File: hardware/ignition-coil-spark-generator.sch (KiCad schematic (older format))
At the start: 16 parts

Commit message: Smaller resistors, trying to make optocoupler act faster
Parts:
- R?: value 10 k -> 270
- R?: value 1 k -> 270
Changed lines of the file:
@@
 P 6000 3750
 F 0 "R?" V 6080 3750 50  0000 C CNN
-F 1 "10 k" V 6000 3750 50  0000 C CNN
+F 1 "270" V 6000 3750 50  0000 C CNN
 F 2 "" V 5930 3750 50  0000 C CNN
 F 3 "" H 6000 3750 50  0000 C CNN
@@
 P 4750 4200
 F 0 "R?" V 4830 4200 50  0000 C CNN
-F 1 "1 k" V 4750 4200 50  0000 C CNN
+F 1 "270" V 4750 4200 50  0000 C CNN
 F 2 "" V 4680 4200 50  0000 C CNN
 F 3 "" H 4750 4200 50  0000 C CNN
@@
 $EndComp
 Wire Wire Line
-	5850 3900 6200 3900
+	5850 3900 6000 3900
+Wire Wire Line
+	6000 3900 6200 3900
 $Comp
 L +9V #PWR?

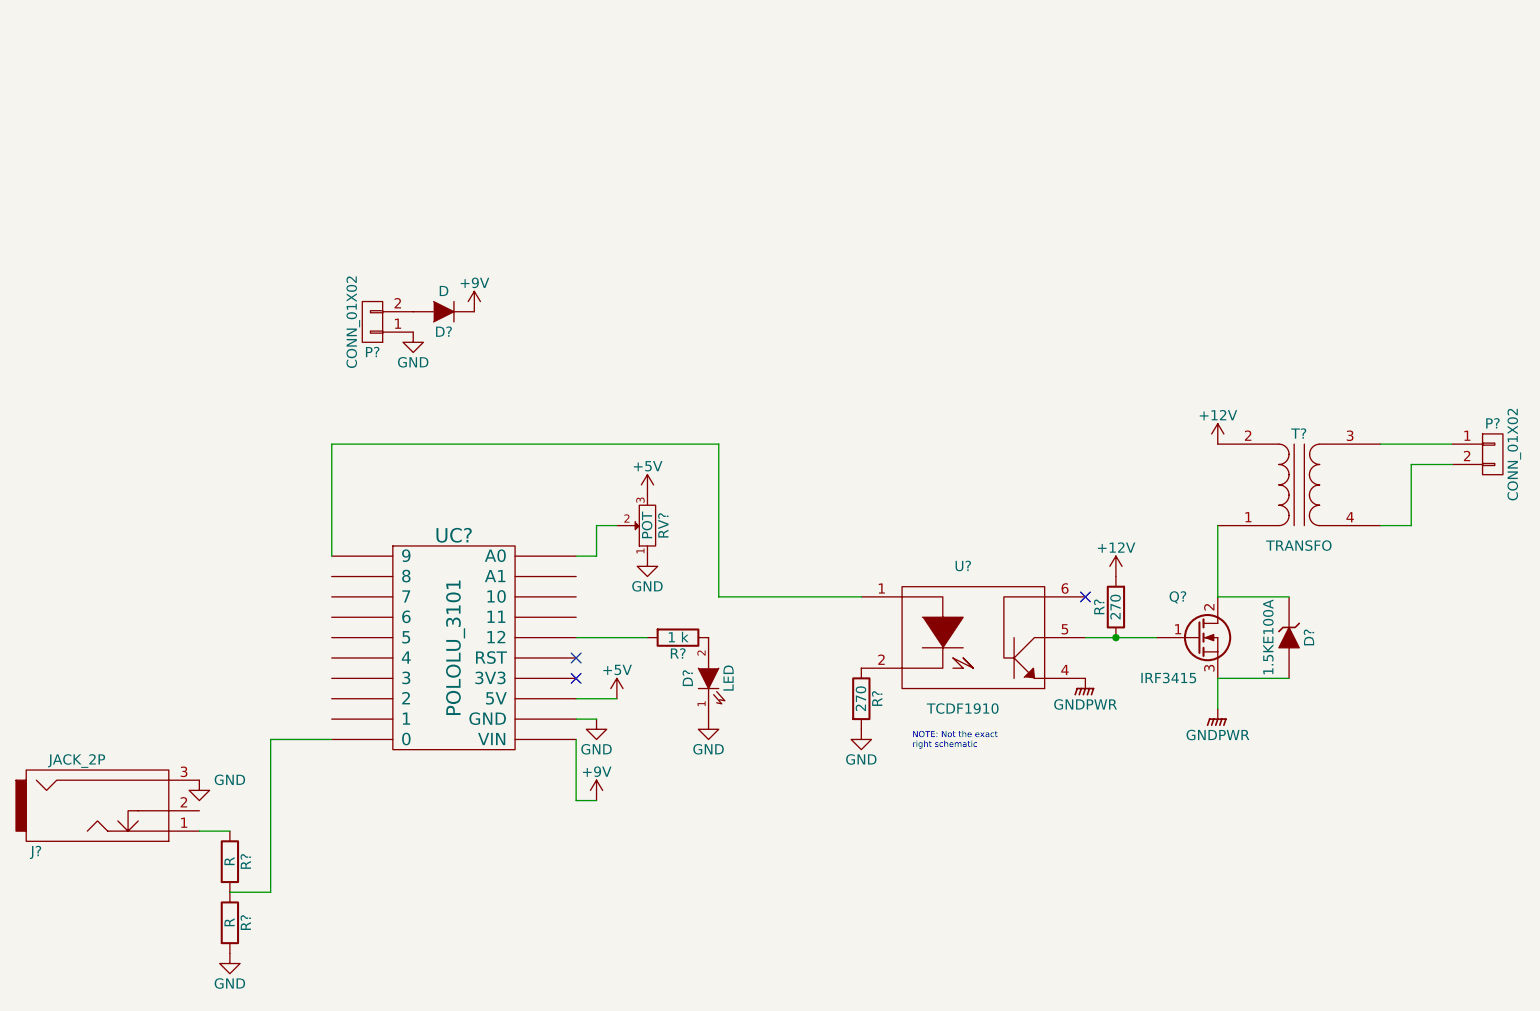
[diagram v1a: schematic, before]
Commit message: New schematic for simplified double ladder generator
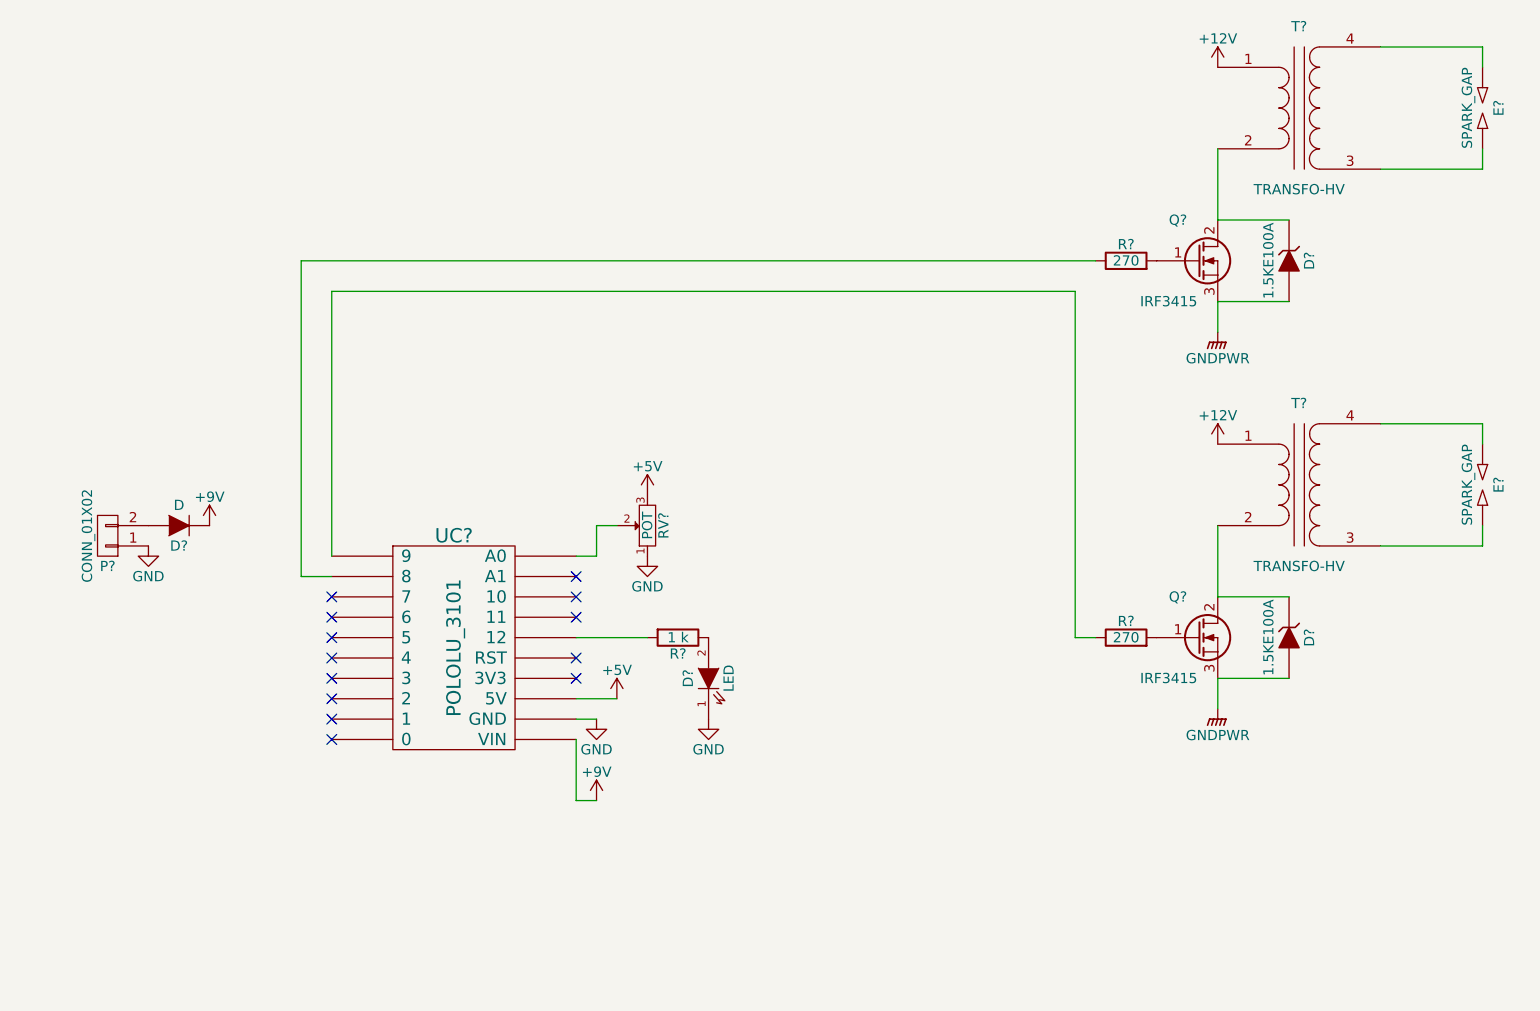
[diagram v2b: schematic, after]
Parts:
- removed J?: JACK_2P, symbol JACK_2P
- removed P?: CONN_01X02, symbol CONN_01X02
- removed R?: 270, symbol R
- removed R? (x2): R, symbol R
- removed T?: TRANSFO, symbol TRANSFO
- removed U?: TCDF1910, symbol PHTRANS
- added D?: 1.5KE100A, symbol ZENER
- added E? (x2): SPARK_GAP, symbol SPARK_GAP
- added Q?: IRF3415, symbol Q_NMOS_GDS
- added R?: 270, symbol R
- added T? (x2): TRANSFO-HV, symbol TRANSFO-HV
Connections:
- net +12V: now also T?.1 (AA), T?.1 (AA); no longer R?.2
- net GNDPWR: now also D?.2 (A), Q?.3 (S)
- net at Q?.1 (G): now also R?.2; no longer R?.1
- net at D?.1 (K), Q?.2 (D): now also T?.2 (AB)
- net at UC?.1 (9): now also R?.1
- net at UC?.2 (8): now also R?.1
- new net: E?.2, T?.3 (SA) (x2)
- new net: E?.1, T?.4 (SB) (x2)
- new net: Q?.1 (G), R?.2
- new net: D?.1 (K), Q?.2 (D), T?.2 (AB)
- no-connect marks 3 -> 13
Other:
- note removed: "NOTE: Not the exact\nright schematic"
- moved on the sheet: D?, P?, R?

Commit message: Updated to run two sparks with configurable charge time
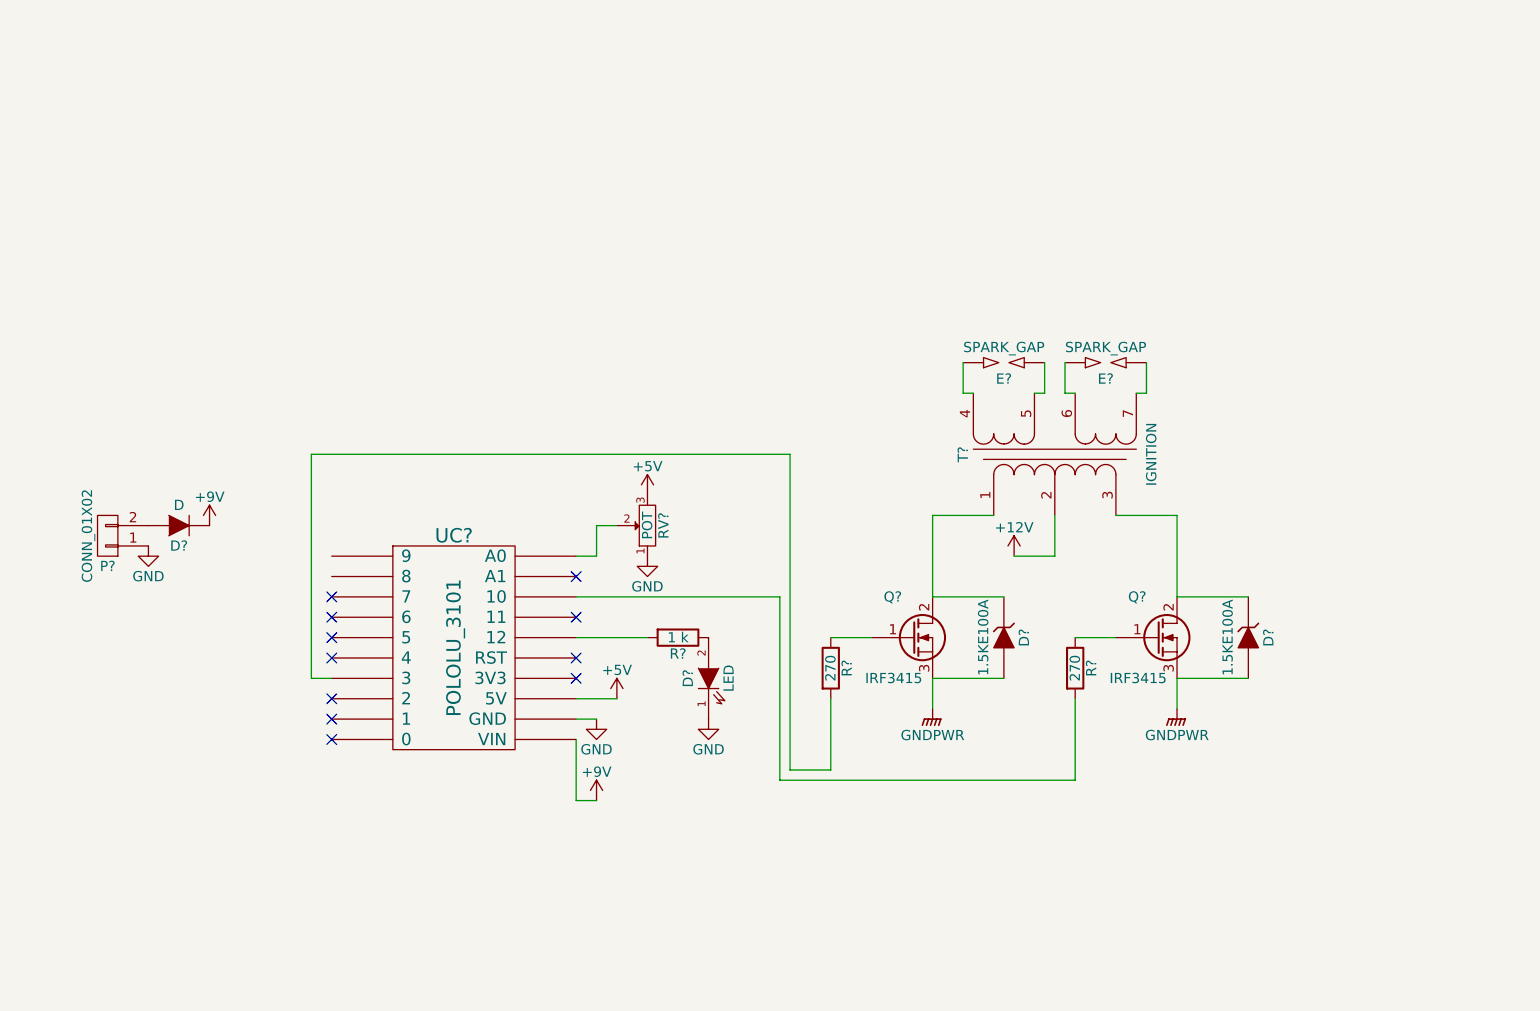
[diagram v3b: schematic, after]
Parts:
- removed T? (x2): TRANSFO-HV, symbol TRANSFO-HV
- added T?: IGNITION, symbol IGNITION
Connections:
- net +12V: now also T?.2
- net at Q?.1 (G): now also R?.1; no longer R?.2 (x2)
- net at D?.1 (K), Q?.2 (D): now also T?.1
- net at UC?.1 (9): no longer R?.1
- net at UC?.2 (8): no longer R?.1
- net at UC?.28 (10): now also R?.2
- net at UC?.7 (3): now also R?.2
- net at E?.2: now also T?.4
- net at E?.1: now also T?.5
- net at D?.1 (K), Q?.2 (D): now also T?.3
- net at E?.2: now also T?.6
- net at E?.1: now also T?.7
- no-connect marks 13 -> 11
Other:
- moved on the sheet: D?, E?, Q?, R?

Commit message: Update schematic to match new, more complete design
1. Indicator leds for the spark outputs
2. Separate power inputs for logic and spark parts
3. Reset button
4. Cleanup
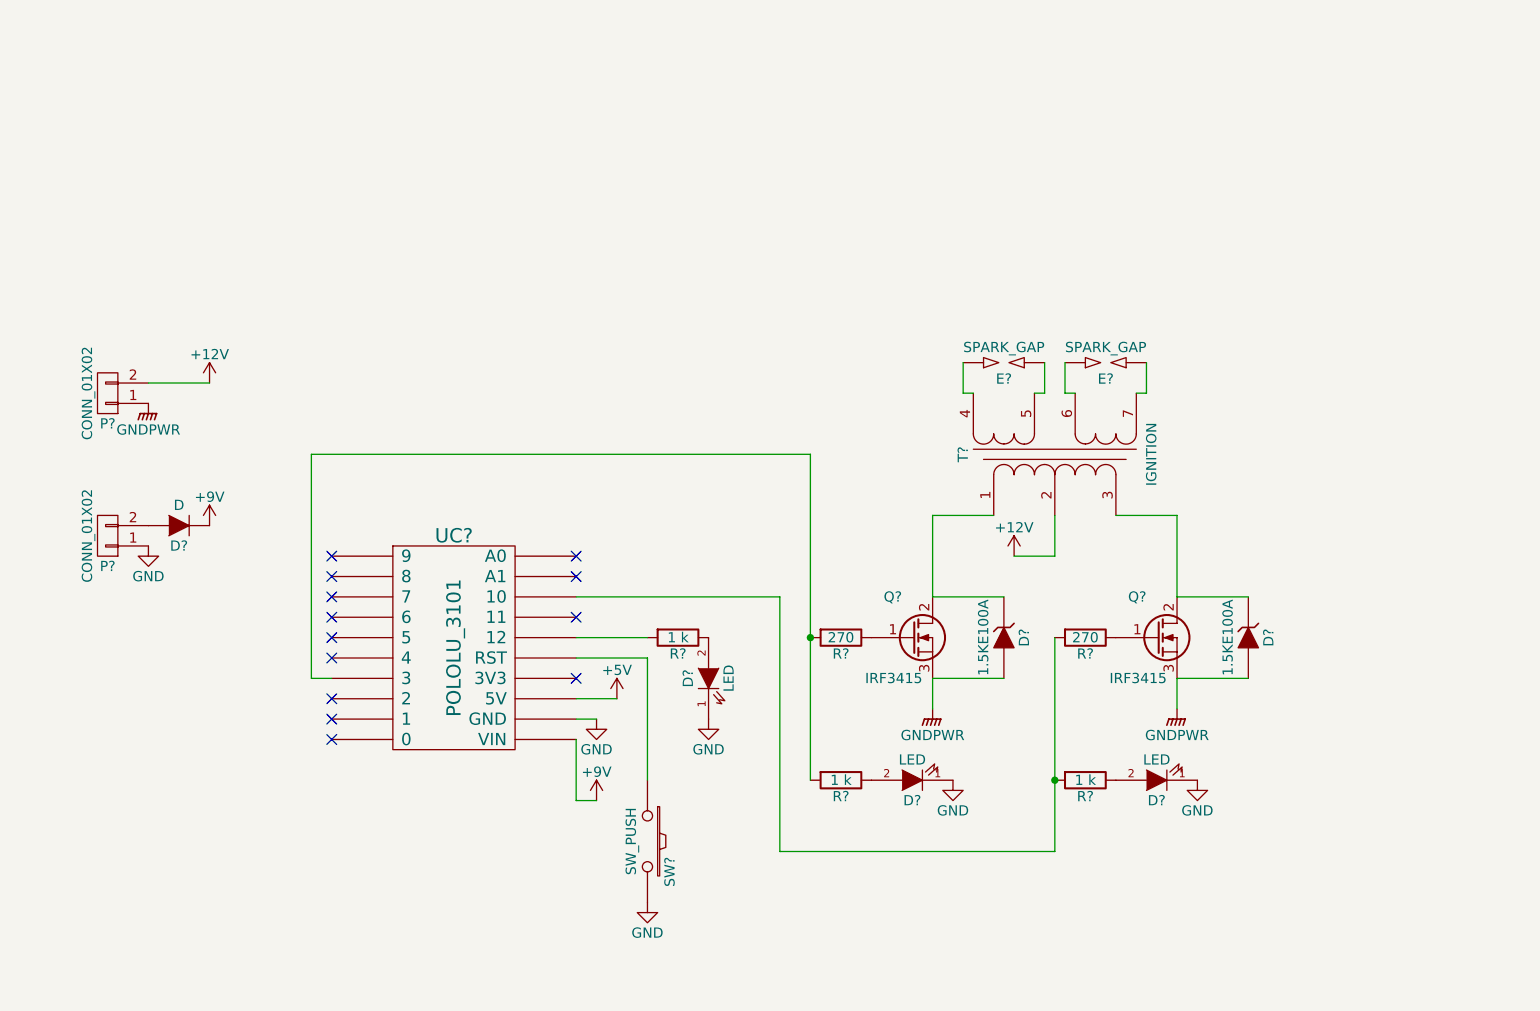
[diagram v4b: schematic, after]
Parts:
- removed RV?: POT, symbol POT
- added D? (x2): LED, symbol LED
- added P?: CONN_01X02, symbol CONN_01X02
- added R? (x2): 1 k, symbol R
- added SW?: SW_PUSH, symbol SW_PUSH
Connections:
- net +12V: now also P?.2 (P2)
- net GND: now also D?.1 (K), D?.1 (K), SW?.2
- net GNDPWR: now also P?.1 (P1)
- net at R?.2, UC?.7 (3): now also R?.2
- net at UC?.25 (RST): now also SW?.1
- net at R?.2, UC?.28 (10): now also R?.2
- new net: D?.2 (A), R?.1 (x2)
- no-connect marks 11 -> 13
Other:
- moved on the sheet: R?
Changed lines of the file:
@@
 L R R?
 U 1 1 5911BDC4
-P 4600 4050
-F 0 "R?" V 4680 4050 50  0000 C CNN
-F 1 "270" V 4600 4050 50  0000 C CNN
-F 2 "" V 4530 4050 50  0000 C CNN
-F 3 "" H 4600 4050 50  0000 C CNN
-	1    4600 4050
-	1    0    0    -1
+P 4650 3900
+F 0 "R?" V 4730 3900 50  0000 C CNN
+F 1 "270" V 4650 3900 50  0000 C CNN
+F 2 "" V 4580 3900 50  0000 C CNN
+F 3 "" H 4650 3900 50  0000 C CNN
+	1    4650 3900
+	0    1    1    0
 $EndComp
 Wire Wire Line
@@
 	1    0    0    -1
 $EndComp
-NoConn ~ 3350 4000
 NoConn ~ 3350 4100
-$Comp
-L POT RV?
-U 1 1 5911E9BB
-P 3700 3350
-F 0 "RV?" H 3700 3270 50  0000 C CNN
-F 1 "POT" H 3700 3350 50  0000 C CNN
-F 2 "" H 3700 3350 50  0000 C CNN
-F 3 "" H 3700 3350 50  0000 C CNN
-	1    3700 3350
-	0    -1   -1   0
-$EndComp
-$Comp
-L GND #PWR?
-U 1 1 5911EAF8
-P 3700 3500
-F 0 "#PWR?" H 3700 3250 50  0001 C CNN
-F 1 "GND" H 3700 3350 50  0000 C CNN
-F 2 "" H 3700 3500 50  0000 C CNN
-F 3 "" H 3700 3500 50  0000 C CNN
-	1    3700 3500
-	1    0    0    -1
-$EndComp
-$Comp
-L +5V #PWR?
-U 1 1 5911EB1E
-P 3700 3200
-F 0 "#PWR?" H 3700 3050 50  0001 C CNN
-F 1 "+5V" H 3700 3340 50  0000 C CNN
-F 2 "" H 3700 3200 50  0000 C CNN
-F 3 "" H 3700 3200 50  0000 C CNN
-	1    3700 3200
-	1    0    0    -1
-$EndComp
 $Comp
 L +5V #PWR?
@@
 Wire Wire Line
 	3350 4200 3550 4200
-Wire Wire Line
-	3350 3500 3450 3500
-Wire Wire Line
-	3450 3500 3450 3350
-Wire Wire Line
-	3450 3350 3550 3350
 $Comp
 L CONN_01X02 P?
@@
 L R R?
 U 1 1 593D2A8C
-P 5800 4050
-F 0 "R?" V 5880 4050 50  0000 C CNN
-F 1 "270" V 5800 4050 50  0000 C CNN
-F 2 "" V 5730 4050 50  0000 C CNN
-F 3 "" H 5800 4050 50  0000 C CNN
-	1    5800 4050
-	1    0    0    -1
+P 5850 3900
+F 0 "R?" V 5930 3900 50  0000 C CNN
+F 1 "270" V 5850 3900 50  0000 C CNN
+F 2 "" V 5780 3900 50  0000 C CNN
+F 3 "" H 5850 3900 50  0000 C CNN
+	1    5850 3900
+	0    1    1    0
 $EndComp
 Wire Wire Line
@@
 	-1   0    0    1
 $EndComp
-Wire Wire Line
-	4400 3000 4400 4550
 NoConn ~ 3350 3800
 NoConn ~ 3350 3600
@@
 $EndComp
 Wire Wire Line
-	4400 4550 4600 4550
-Wire Wire Line
-	4600 4550 4600 4200
-Wire Wire Line
-	4600 3900 4800 3900
-Wire Wire Line
-	5800 4200 5800 4600
-Wire Wire Line
-	5800 3900 6000 3900
+	4600 4850 4600 4850
 Wire Wire Line
 	6300 3300 6000 3300
@@
 	5250 2700 5250 2550
 Wire Wire Line
-	2050 3000 4400 3000
+	2050 3000 4500 3000
 Wire Wire Line
 	3350 3700 4350 3700
 Wire Wire Line
-	4350 3700 4350 4600
-Wire Wire Line
-	4350 4600 5800 4600
+	4350 3700 4350 4950
+Wire Wire Line
+	4350 4950 5700 4950
 Wire Wire Line
 	2150 4100 2050 4100
 Wire Wire Line
 	2050 4100 2050 3000
+$Comp
+L LED D?
+U 1 1 595437D4
+P 5000 4600
+F 0 "D?" H 5000 4700 50  0000 C CNN
+F 1 "LED" H 5000 4500 50  0000 C CNN
+F 2 "" H 5000 4600 50  0000 C CNN
+F 3 "" H 5000 4600 50  0000 C CNN
+	1    5000 4600
+	-1   0    0    1
+$EndComp
+$Comp
+L R R?
+U 1 1 5954383B
+P 4650 4600
+F 0 "R?" V 4730 4600 50  0000 C CNN
+F 1 "1 k" V 4650 4600 50  0000 C CNN
+F 2 "" V 4580 4600 50  0000 C CNN
+F 3 "" H 4650 4600 50  0000 C CNN
+	1    4650 4600
+	0    1    1    0
+$EndComp
+$Comp
+L GND #PWR?
+U 1 1 59543C06
+P 5200 4600
+F 0 "#PWR?" H 5200 4350 50  0001 C CNN
+F 1 "GND" H 5200 4450 50  0000 C CNN
+F 2 "" H 5200 4600 50  0000 C CNN
+F 3 "" H 5200 4600 50  0000 C CNN
+	1    5200 4600
+	1    0    0    -1
+$EndComp
+Wire Wire Line
+	4500 3000 4500 4600
+Connection ~ 4500 3900
+$Comp
+L LED D?
+U 1 1 59543F6A
+P 6200 4600
+F 0 "D?" H 6200 4700 50  0000 C CNN
+F 1 "LED" H 6200 4500 50  0000 C CNN
+F 2 "" H 6200 4600 50  0000 C CNN
+F 3 "" H 6200 4600 50  0000 C CNN
+	1    6200 4600
+	-1   0    0    1
+$EndComp
+$Comp
+L R R?
+U 1 1 59543F70
+P 5850 4600
+F 0 "R?" V 5930 4600 50  0000 C CNN
+F 1 "1 k" V 5850 4600 50  0000 C CNN
+F 2 "" V 5780 4600 50  0000 C CNN
+F 3 "" H 5850 4600 50  0000 C CNN
+	1    5850 4600
+	0    1    1    0
+$EndComp
+$Comp
+L GND #PWR?
+U 1 1 59543F76
+P 6400 4600
+F 0 "#PWR?" H 6400 4350 50  0001 C CNN
+F 1 "GND" H 6400 4450 50  0000 C CNN
+F 2 "" H 6400 4600 50  0000 C CNN
+F 3 "" H 6400 4600 50  0000 C CNN
+	1    6400 4600
+	1    0    0    -1
+$EndComp
+Wire Wire Line
+	5700 4950 5700 3900
+Connection ~ 5700 4600
+$Comp
+L SW_PUSH SW?
+U 1 1 59544EE5
+P 3700 4900
+F 0 "SW?" H 3850 5010 50  0000 C CNN
+F 1 "SW_PUSH" H 3700 4820 50  0000 C CNN
+F 2 "" H 3700 4900 50  0000 C CNN
+F 3 "" H 3700 4900 50  0000 C CNN
+	1    3700 4900
+	0    1    1    0
+$EndComp
+Wire Wire Line
+	3350 4000 3700 4000
+Wire Wire Line
+	3700 4000 3700 4600
+$Comp
+L GND #PWR?
+U 1 1 5954501D
+P 3700 5200
+F 0 "#PWR?" H 3700 4950 50  0001 C CNN
+F 1 "GND" H 3700 5050 50  0000 C CNN
+F 2 "" H 3700 5200 50  0000 C CNN
+F 3 "" H 3700 5200 50  0000 C CNN
+	1    3700 5200
+	1    0    0    -1
+$EndComp
+NoConn ~ 3350 3500
+$Comp
+L CONN_01X02 P?
+U 1 1 5954546E
+P 1050 2700
+F 0 "P?" H 1050 2850 50  0000 C CNN
+F 1 "CONN_01X02" V 1150 2700 50  0000 C CNN
+F 2 "" H 1050 2700 50  0000 C CNN
+F 3 "" H 1050 2700 50  0000 C CNN
+	1    1050 2700
+	-1   0    0    1
+$EndComp
+Wire Wire Line
+	1250 2650 1550 2650
+$Comp
+L GNDPWR #PWR?
+U 1 1 5954555D
+P 1250 2750
+F 0 "#PWR?" H 1250 2550 50  0001 C CNN
+F 1 "GNDPWR" H 1250 2620 50  0000 C CNN
+F 2 "" H 1250 2700 50  0000 C CNN
+F 3 "" H 1250 2700 50  0000 C CNN
+	1    1250 2750
+	1    0    0    -1
+$EndComp
+$Comp
+L +12V #PWR?
+U 1 1 59545599
+P 1550 2650
+F 0 "#PWR?" H 1550 2500 50  0001 C CNN
+F 1 "+12V" H 1550 2790 50  0000 C CNN
+F 2 "" H 1550 2650 50  0000 C CNN
+F 3 "" H 1550 2650 50  0000 C CNN
+	1    1550 2650
+	1    0    0    -1
+$EndComp
+NoConn ~ 2150 3600
+NoConn ~ 2150 3500
 $EndSCHEMATC
